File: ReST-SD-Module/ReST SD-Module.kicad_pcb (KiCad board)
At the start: 2 copper layers, 18.7 x 28.7 mm, 25 parts

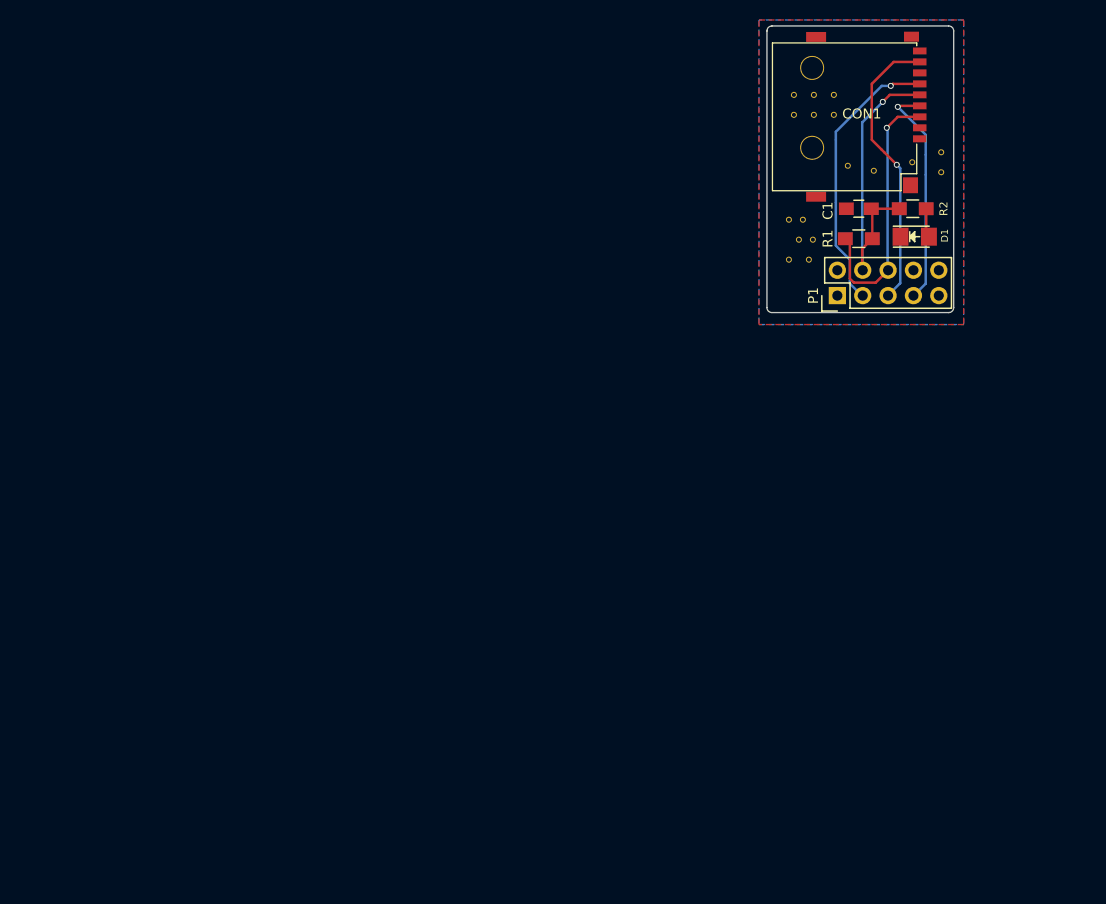
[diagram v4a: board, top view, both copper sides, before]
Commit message: updated SD Card module
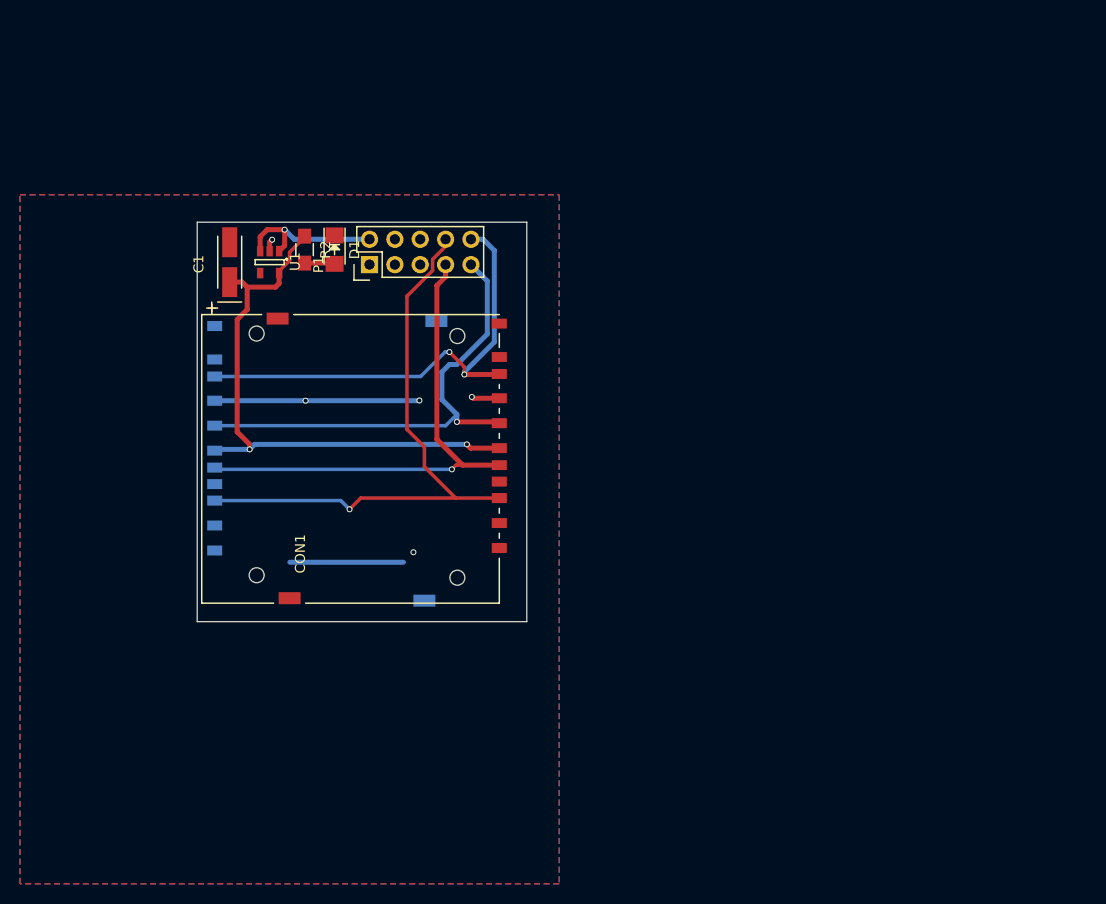
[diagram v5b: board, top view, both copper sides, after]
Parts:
- removed ? (x17): , ReST-Library:VIA-0.6mm
- removed ?: , ReST-Library:Logo_silk_OSHW_6x6mm
- removed ?: , ReST-Library:STM32-6mm
- removed R1: , Resistors_SMD:R_0805_HandSoldering
- added CON2: uSD_Card, Connect:SD_Card_Receptacle, B.Cu at (79.5, 124.2)
- added U1: MIC5205, TO_SOT_Packages_SMD:SOT-23-5, F.Cu at (85.0, 104.8)
- C1: value (none) -> CP1_Small; footprint Capacitors_SMD:C_0805_HandSoldering -> Capacitors_Tantalum_SMD:TantalC_SizeA_EIA-3216_HandSoldering
- CON1: value (none) -> uSD_Card; footprint ReST-Library:uSD -> Connect:SD_Card_Receptacle
- D1: value (none) -> Led_Small
- P1: value (none) -> CONN_02X05
- R2: value (none) -> 1K
- moved C1 63.2 mm to (81.0, 104.8), turned to 90 degrees
- moved R2 61.0 mm to (88.5, 103.5), turned to 270 degrees
- moved D1 58.1 mm to (91.5, 103.5), turned to 270 degrees
- moved CON1 53.8 mm to (108.0, 124.0), turned to 270 degrees
- moved P1 47.0 mm to (95.0, 105.0)
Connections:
- P1 pad 10: (no net) -> /SPI-MISO
- P1 pad 2: (no net) -> +5V
- P1 pad 3: /SPI-SCK -> (no net)
- P1 pad 4: +3V3 -> (no net)
- P1 pad 5: /SPI-MISO -> (no net)
- P1 pad 6: /SPI-CS -> (no net)
- P1 pad 8: (no net) -> /SPI-CS
- P1 pad 9: (no net) -> /SPI-SCK
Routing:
- net GND: track 0.00 -> 35.9 mm, vias 0 -> 5
- net /SPI-CS: track 26.9 -> 58.9 mm
- net /SPI-MOSI: track 22.9 -> 50.3 mm
- net +3V3: track 31.3 -> 57.2 mm, vias 1 -> 2
- net /SPI-SCK: track 28.2 -> 48.4 mm
- net /SPI-MISO: track 28.7 -> 47.4 mm, vias 1 -> 2
- net +5V: track 0.00 -> 15.5 mm, vias 0 -> 1
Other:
- board size 18.7 x 28.7 mm -> 33 x 40 mm
- net class Default: trace_width 0.25 -> 0.3
- board text removed: "ReST SD Card Adapter Rev. A @maker_berry"

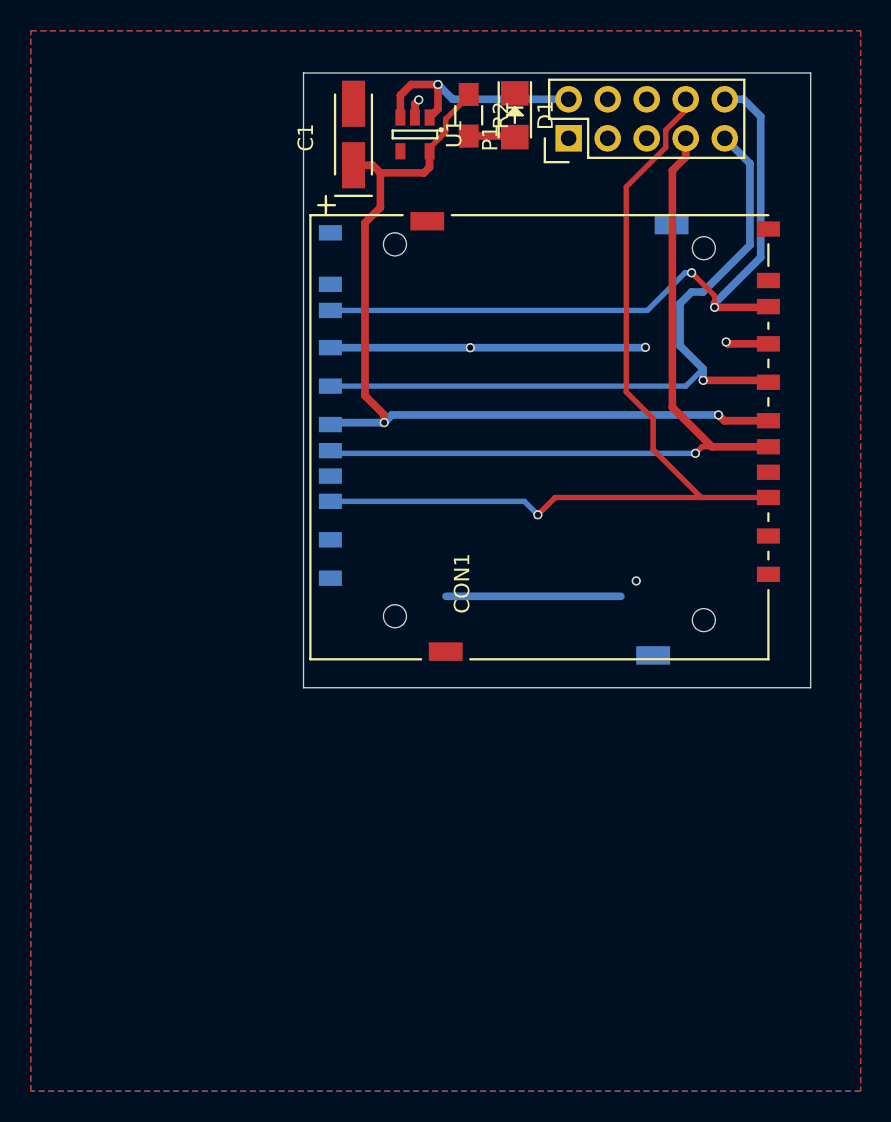
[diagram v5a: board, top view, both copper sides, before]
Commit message: Final Release
With Mainboard, SD Card Adapter and Adapter for a RepRapDiscount Full Graphic Smart Controller
The SD Card Socket can be soldered on the front or on the back, so that the user can insert the card either from top or from the botton, depending on how the controller is mounted.
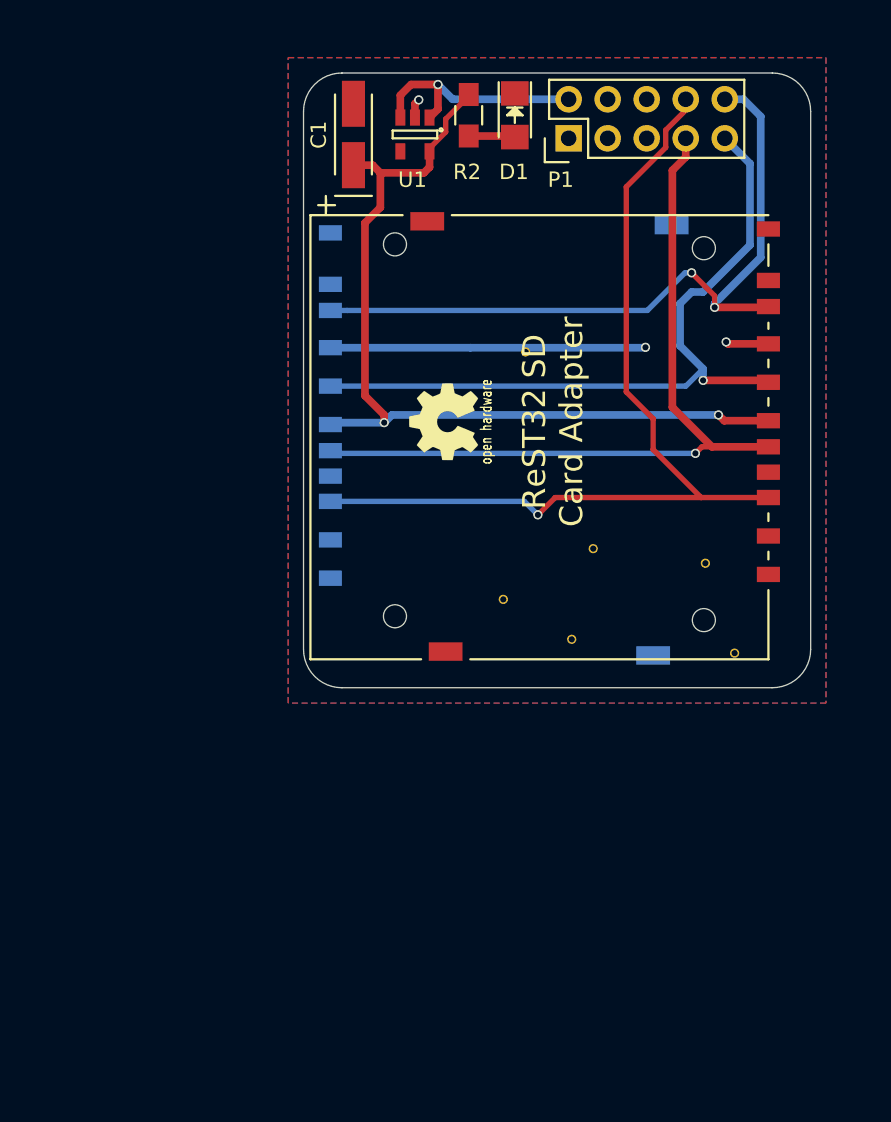
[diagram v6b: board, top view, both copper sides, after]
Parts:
- added G***: LOGO, ReST-Library:Logo_silk_OSHW_6x6mm, B.Cu at (86.9, 123.4)
- added G***: LOGO, ReST-Library:Logo_silk_OSHW_6x6mm, F.Cu at (86.9, 123.4)
- added REF**: 1pin, ReST-Library:1pin, F.Cu at (96.6, 131.7)
- added REF**: 1pin, ReST-Library:1pin, F.Cu at (90.8, 135.0)
- added REF**: 1pin, ReST-Library:1pin, F.Cu at (103.9, 132.7)
- added REF**: 1pin, ReST-Library:1pin, F.Cu at (105.8, 138.5)
- added REF**: 1pin, ReST-Library:1pin, F.Cu at (92.2, 118.9)
- added REF**: 1pin, ReST-Library:1pin, F.Cu at (95.2, 137.6)
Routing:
- net GND: track 35.9 -> 24.6 mm, vias 5 -> 3
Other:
- outline, holes or cut-outs redrawn
- board text added: "ReST32 SD Card Adapter"

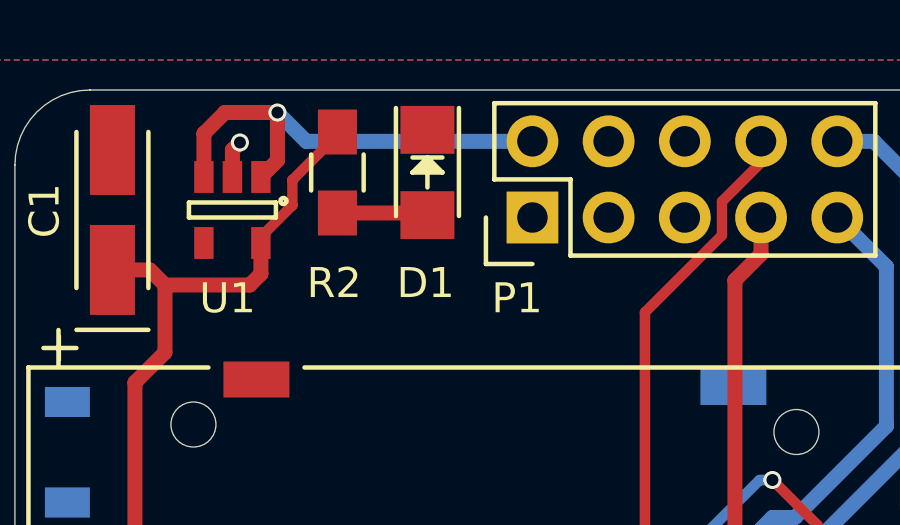
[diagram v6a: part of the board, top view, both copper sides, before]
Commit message: minor changes to values of components and footprints. added two leds for both 12V Rails.
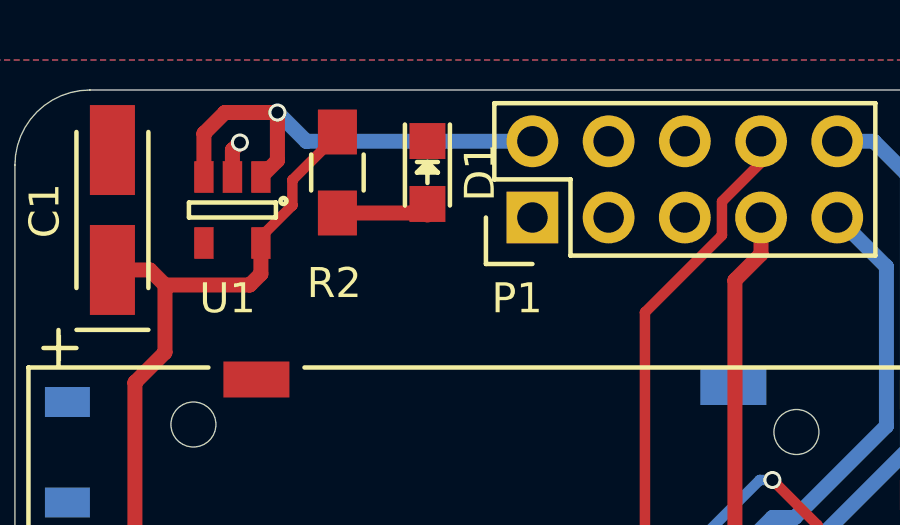
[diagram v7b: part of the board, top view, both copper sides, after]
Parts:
- C1: value CP1_Small -> 2.2uF
- D1: footprint LEDs:LED_1206 -> LEDs:LED_0805
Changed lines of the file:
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@@
 (kicad_pcb (version 4) (host pcbnew 4.0.2-stable)
   (general
-    (links 0)
-    (no_connects 0)
-    (area 77.744999 100.744999 110.755001 140.755001)
+    (links 34)
+    (no_connects 1)
+    (area 66.724999 99.439285 120.775001 141.750001)
     (thickness 1.6)
     (drawings 10)
@@
       (effects (font (size 1 1) (thickness 0.15)))
     )
-    (fp_text value CP1_Small (at -0.09906 3.0988 90) (layer F.Fab)
+    (fp_text value 2.2uF (at -0.09906 3.0988 90) (layer F.Fab)
       (effects (font (size 1 1) (thickness 0.15)))
     )
@@
     (pad "" np_thru_hole circle (at -12.1 24.3 270) (size 1.5 1.5) (drill 1.5) (layers *.Cu *.Mask F.SilkS)
       (zone_connect 2))
-  )
-  (module LEDs:LED_1206 (layer F.Cu)
-    (at 91.5 103.5 270)
-    (descr "LED 1206 smd package")
-    (tags "LED1206 SMD")
-    (attr smd)
-    (fp_text reference D1 (at 3.688 0.06 360) (layer F.SilkS)
-      (effects (font (size 1 1) (thickness 0.15)))
-    )
-    (fp_text value Led_Small (at 0 2 270) (layer F.Fab)
-      (effects (font (size 1 1) (thickness 0.15)))
-    )
-    (fp_line (start -2.15 1.05) (end 1.45 1.05) (layer F.SilkS) (width 0.15))
-    (fp_line (start -2.15 -1.05) (end 1.45 -1.05) (layer F.SilkS) (width 0.15))
-    (fp_line (start -0.1 -0.3) (end -0.1 0.3) (layer F.SilkS) (width 0.15))
-    (fp_line (start -0.1 0.3) (end -0.4 0) (layer F.SilkS) (width 0.15))
-    (fp_line (start -0.4 0) (end -0.2 -0.2) (layer F.SilkS) (width 0.15))
-    (fp_line (start -0.2 -0.2) (end -0.2 0.05) (layer F.SilkS) (width 0.15))
-    (fp_line (start -0.2 0.05) (end -0.25 0) (layer F.SilkS) (width 0.15))
-    (fp_line (start -0.5 -0.5) (end -0.5 0.5) (layer F.SilkS) (width 0.15))
-    (fp_line (start 0 0) (end 0.5 0) (layer F.SilkS) (width 0.15))
-    (fp_line (start -0.5 0) (end 0 -0.5) (layer F.SilkS) (width 0.15))
-    (fp_line (start 0 -0.5) (end 0 0.5) (layer F.SilkS) (width 0.15))
-    (fp_line (start 0 0.5) (end -0.5 0) (layer F.SilkS) (width 0.15))
-    (fp_line (start 2.5 -1.25) (end -2.5 -1.25) (layer F.CrtYd) (width 0.05))
-    (fp_line (start -2.5 -1.25) (end -2.5 1.25) (layer F.CrtYd) (width 0.05))
-    (fp_line (start -2.5 1.25) (end 2.5 1.25) (layer F.CrtYd) (width 0.05))
-    (fp_line (start 2.5 1.25) (end 2.5 -1.25) (layer F.CrtYd) (width 0.05))
-    (pad 2 smd rect (at 1.41986 0 90) (size 1.59766 1.80086) (layers F.Cu F.Paste F.Mask)
-      (net 7 "Net-(D1-Pad2)"))
-    (pad 1 smd rect (at -1.41986 0 90) (size 1.59766 1.80086) (layers F.Cu F.Paste F.Mask)
-      (net 2 GND))
-    (model LEDs.3dshapes/LED_1206.wrl
-      (at (xyz 0 0 0))
-      (scale (xyz 1 1 1))
-      (rotate (xyz 0 0 180))
-    )
   )
   (module Pin_Headers:Pin_Header_Straight_2x05 (layer F.Cu)
@@
       (xy -1.51384 2.24536)) (layer F.SilkS) (width 0.00254))
   )
+  (module LEDs:LED_0805 (layer F.Cu)
+    (at 91.5 103.5 270)
+    (descr "LED 0805 smd package")
+    (tags "LED 0805 SMD")
+    (attr smd)
+    (fp_text reference D1 (at 0 -1.75 270) (layer F.SilkS)
+      (effects (font (size 1 1) (thickness 0.15)))
+    )
+    (fp_text value Led_Small (at 0 1.75 270) (layer F.Fab)
+      (effects (font (size 1 1) (thickness 0.15)))
+    )
+    (fp_line (start -1.6 0.75) (end 1.1 0.75) (layer F.SilkS) (width 0.15))
+    (fp_line (start -1.6 -0.75) (end 1.1 -0.75) (layer F.SilkS) (width 0.15))
+    (fp_line (start -0.1 0.15) (end -0.1 -0.1) (layer F.SilkS) (width 0.15))
+    (fp_line (start -0.1 -0.1) (end -0.25 0.05) (layer F.SilkS) (width 0.15))
+    (fp_line (start -0.35 -0.35) (end -0.35 0.35) (layer F.SilkS) (width 0.15))
+    (fp_line (start 0 0) (end 0.35 0) (layer F.SilkS) (width 0.15))
+    (fp_line (start -0.35 0) (end 0 -0.35) (layer F.SilkS) (width 0.15))
+    (fp_line (start 0 -0.35) (end 0 0.35) (layer F.SilkS) (width 0.15))
+    (fp_line (start 0 0.35) (end -0.35 0) (layer F.SilkS) (width 0.15))
+    (fp_line (start 1.9 -0.95) (end 1.9 0.95) (layer F.CrtYd) (width 0.05))
+    (fp_line (start 1.9 0.95) (end -1.9 0.95) (layer F.CrtYd) (width 0.05))
+    (fp_line (start -1.9 0.95) (end -1.9 -0.95) (layer F.CrtYd) (width 0.05))
+    (fp_line (start -1.9 -0.95) (end 1.9 -0.95) (layer F.CrtYd) (width 0.05))
+    (pad 2 smd rect (at 1.04902 0 90) (size 1.19888 1.19888) (layers F.Cu F.Paste F.Mask)
+      (net 7 "Net-(D1-Pad2)"))
+    (pad 1 smd rect (at -1.04902 0 90) (size 1.19888 1.19888) (layers F.Cu F.Paste F.Mask)
+      (net 2 GND))
+    (model LEDs.3dshapes/LED_0805.wrl
+      (at (xyz 0 0 0))
+      (scale (xyz 1 1 1))
+      (rotate (xyz 0 0 0))
+    )
+  )
   (gr_text "ReST32 SD\nCard Adapter" (at 93.98 123.444 90) (layer F.SilkS)
